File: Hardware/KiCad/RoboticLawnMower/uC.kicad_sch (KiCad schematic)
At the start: 9 parts, among them J12 Conn_02x05_Row_Letter_Last, U2 AVR128DB48x-xPT, Y1 32.768kHz

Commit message: Layout
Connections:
- net CURR_ALERT_CHRG: no longer names the net of U2.4 (PB0)
- net CURR_ALERT_M1: no longer names the net of U2.11 (PC1)
- net CURR_ALERT_M2: no longer names the net of U2.10 (PC0)
- net CURR_ALERT_M3: no longer names the net of U2.9 (PB5)
- net CURR_ALERT_M4: no longer names the net of U2.8 (PB4)
- net CURR_ALERT_M5: no longer names the net of U2.5 (PB1)
- net CURR_ALERT_SYS: no longer names the net of U2.3 (PA7)
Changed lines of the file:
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@@
   (junction (at 233.68 119.38) (diameter 0) (color 0 0 0 0)
-  )
-  (bus_entry (at 283.21 114.3) (size 2.54 2.54)
-    (stroke (width 0) (type default) (color 0 0 0 0))
-  )
-  (bus_entry (at 283.21 116.84) (size 2.54 2.54)
-    (stroke (width 0) (type default) (color 0 0 0 0))
-  )
-  (bus_entry (at 283.21 109.22) (size 2.54 2.54)
-    (stroke (width 0) (type default) (color 0 0 0 0))
-  )
-  (bus_entry (at 283.21 132.08) (size 2.54 2.54)
-    (stroke (width 0) (type default) (color 0 0 0 0))
-  )
-  (bus_entry (at 283.21 134.62) (size 2.54 2.54)
-    (stroke (width 0) (type default) (color 0 0 0 0))
-  )
-  (bus_entry (at 283.21 127) (size 2.54 2.54)
-    (stroke (width 0) (type default) (color 0 0 0 0))
-  )
-  (bus_entry (at 283.21 124.46) (size 2.54 2.54)
-    (stroke (width 0) (type default) (color 0 0 0 0))
   )
   (wire (pts (xy 100.33 60.96) (xy 110.49 60.96))
@@
   )
   (wire (pts (xy 233.68 71.12) (xy 233.68 72.39))
-    (stroke (width 0) (type default) (color 0 0 0 0))
-  )
-  (bus (pts (xy 285.75 129.54) (xy 285.75 134.62))
     (stroke (width 0) (type default) (color 0 0 0 0))
   )
@@
     (stroke (width 0) (type default) (color 0 0 0 0))
   )
-  (wire (pts (xy 220.98 114.3) (xy 283.21 114.3))
-    (stroke (width 0) (type default) (color 0 0 0 0))
-  )
-  (bus (pts (xy 285.75 116.84) (xy 285.75 119.38))
-    (stroke (width 0) (type default) (color 0 0 0 0))
-  )
   (wire (pts (xy 57.15 44.45) (xy 57.15 48.26))
     (stroke (width 0) (type default) (color 0 0 0 0))
@@
   )
   (wire (pts (xy 220.98 139.7) (xy 266.7 139.7))
-    (stroke (width 0) (type default) (color 0 0 0 0))
-  )
-  (wire (pts (xy 220.98 109.22) (xy 283.21 109.22))
     (stroke (width 0) (type default) (color 0 0 0 0))
   )
@@
     (stroke (width 0) (type default) (color 0 0 0 0))
   )
-  (bus (pts (xy 285.75 134.62) (xy 285.75 137.16))
-    (stroke (width 0) (type default) (color 0 0 0 0))
-  )
   (wire (pts (xy 198.12 163.83) (xy 200.66 163.83))
     (stroke (width 0) (type default) (color 0 0 0 0))
@@
     (stroke (width 0) (type default) (color 0 0 0 0))
   )
-  (wire (pts (xy 220.98 116.84) (xy 283.21 116.84))
-    (stroke (width 0) (type default) (color 0 0 0 0))
-  )
   (wire (pts (xy 87.63 99.06) (xy 180.34 99.06))
-    (stroke (width 0) (type default) (color 0 0 0 0))
-  )
-  (wire (pts (xy 220.98 132.08) (xy 283.21 132.08))
-    (stroke (width 0) (type default) (color 0 0 0 0))
-  )
-  (bus (pts (xy 285.75 119.38) (xy 285.75 127))
     (stroke (width 0) (type default) (color 0 0 0 0))
   )
@@
     (stroke (width 0) (type default) (color 0 0 0 0))
   )
-  (wire (pts (xy 220.98 134.62) (xy 283.21 134.62))
-    (stroke (width 0) (type default) (color 0 0 0 0))
-  )
   (wire (pts (xy 110.49 60.96) (xy 110.49 63.5))
-    (stroke (width 0) (type default) (color 0 0 0 0))
-  )
-  (wire (pts (xy 220.98 124.46) (xy 283.21 124.46))
     (stroke (width 0) (type default) (color 0 0 0 0))
   )
@@
     (stroke (width 0) (type default) (color 0 0 0 0))
   )
-  (bus (pts (xy 285.75 111.76) (xy 285.75 116.84))
-    (stroke (width 0) (type default) (color 0 0 0 0))
-  )
   (wire (pts (xy 220.98 119.38) (xy 233.68 119.38))
     (stroke (width 0) (type default) (color 0 0 0 0))
@@
     (stroke (width 0) (type default) (color 0 0 0 0))
   )
-  (bus (pts (xy 285.75 137.16) (xy 285.75 139.7))
-    (stroke (width 0) (type default) (color 0 0 0 0))
-  )
-  (wire (pts (xy 220.98 127) (xy 283.21 127))
-    (stroke (width 0) (type default) (color 0 0 0 0))
-  )
   (wire (pts (xy 82.55 55.88) (xy 88.9 55.88))
     (stroke (width 0) (type default) (color 0 0 0 0))
   )
   (wire (pts (xy 88.9 55.88) (xy 88.9 72.39))
-    (stroke (width 0) (type default) (color 0 0 0 0))
-  )
-  (bus (pts (xy 285.75 139.7) (xy 295.91 139.7))
     (stroke (width 0) (type default) (color 0 0 0 0))
   )
@@
     (stroke (width 0) (type default) (color 0 0 0 0))
   )
-  (bus (pts (xy 285.75 127) (xy 285.75 129.54))
-    (stroke (width 0) (type default) (color 0 0 0 0))
-  )
-  (label "CURR_ALERT_M3" (at 241.3 127 0)
-    (effects (font (size 1.27 1.27)) (justify left bottom))
-  )
-  (label "CURR_ALERT_M5" (at 241.3 116.84 0)
-    (effects (font (size 1.27 1.27)) (justify left bottom))
-  )
-  (label "CURR_ALERT_SYS" (at 241.3 109.22 0)
-    (effects (font (size 1.27 1.27)) (justify left bottom))
-  )
-  (label "CURR_ALERT_M2" (at 241.3 132.08 0)
-    (effects (font (size 1.27 1.27)) (justify left bottom))
-  )
   (label "AVR_UPDI" (at 45.72 58.42 0)
     (effects (font (size 1.27 1.27)) (justify left bottom))
   )
-  (label "CURR_ALERT_CHRG" (at 241.3 114.3 0)
-    (effects (font (size 1.27 1.27)) (justify left bottom))
-  )
-  (label "CURR_ALERT_M4" (at 241.3 124.46 0)
-    (effects (font (size 1.27 1.27)) (justify left bottom))
-  )
   (label "~{AVR_RERSET}" (at 123.19 60.96 0)
-    (effects (font (size 1.27 1.27)) (justify left bottom))
-  )
-  (label "CURR_ALERT_M1" (at 241.3 134.62 0)
     (effects (font (size 1.27 1.27)) (justify left bottom))
   )
@@
     (effects (font (size 1.27 1.27)) (justify left))
   )
-  (hierarchical_label "MOTOR_CONTROL" (shape bidirectional) (at 295.91 139.7 0)
-    (effects (font (size 1.27 1.27)) (justify left))
-  )

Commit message: LAYOUT
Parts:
- added C11: 5p6, Capacitor_SMD:C_0603_1608Metric, symbol Device:C
- added J18: Conn_02x05_Row_Letter_Last, Connector_PinHeader_1.27mm:PinHeader_2x05_P1.27mm_Vertical_SMD, symbol Connector_Generic:Conn_02x05_Odd_Even
- added R51, R53: 47K, Resistor_SMD:R_0603_1608Metric, symbol Device:R
- added R52: 33R, Resistor_SMD:R_0603_1608Metric, symbol Device:R
- added R54, R55: 4k7, Resistor_SMD:R_0603_1608Metric, symbol Device:R
- added R56, R57, R58, R60, R63: N.P., Resistor_SMD:R_0402_1005Metric, symbol Device:R
- added R59, R61, R62, R64, R65: 10R, Resistor_SMD:R_0402_1005Metric, symbol Device:R
- added U5: AVR128DB48x-xPT, Package_QFP:TQFP-48_7x7mm_P0.5mm, symbol MCU_Microchip_AVR_Dx:AVR128DB48x-xPT
- added Y2: 32.768kHz, Crystal:Crystal_SMD_3215-2Pin_3.2x1.5mm, symbol Device:Crystal
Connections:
- net +3.3V: now also J18.4 (Pin_4), R51.1, R53.1, R54.2, R55.2, U5.14 (VDDIO2), U5.28 (AVDD), U5.42 (VDD)
- net GND: now also C11.2, J18.2 (Pin_2), J18.9 (Pin_9), U5.15 (GND), U5.29 (AGND), U5.43 (GND)
- net I2C_1_SCL: now also R63.2, R64.2; no longer R42.1, U2.7 (PB3)
- net I2C_1_SDA: now also R59.2, R60.2; no longer R41.1, U2.6 (PB2)
- net Motor_M1..4_EN: now also R58.2, R65.2; no longer U2.13 (PC3)
- net Motor_M5_EN: now also R57.2, R62.2; no longer U2.16 (PC4)
- net ~{PCA_9685_OE}: now also R56.2, R61.2; no longer U2.12 (PC2)
- new net: R42.1, R63.1, U2.7 (PB3)
- new net: R56.1, U2.12 (PC2)
- new net: R41.1, R60.1, U2.6 (PB2)
- new net: R57.1, U2.16 (PC4)
- new net: R61.1, U5.12 (PC2)
- new net: R65.1, U5.13 (PC3)
- new net: R62.1, U5.16 (PC4)
- new net: U5.34 (XTAL32K1/PF0), Y2.2
- new net: U5.35 (XTAL32K2/PF1), Y2.1
- new net: R54.1, R59.1, U5.6 (PB2)
- new net: R55.1, R64.1, U5.7 (PB3)
- new net: J18.6 (Pin_6), R52.1
- new net: R58.1, U2.13 (PC3)
- new net AVR_UPDI_1: J18.3 (Pin_3), R51.2, U5.41 (UPDI)
- new net MOTOR_CTR_CTN_0: U5.21 (PD1)
- new net MOTOR_CTR_CTN_1: U5.22 (PD2)
- new net MOTOR_CTR_CTN_2: U5.23 (PD3)
- new net MOTOR_CTR_CTN_3: U5.24 (PD4)
- new net MOTOR_CTR_CTN_4: U5.20 (PD0)
- new net MOTOR_CTR_I2C_0_SCL: U5.47 (PA3)
- new net MOTOR_CTR_I2C_0_SDA: U5.46 (PA2)
- new net MOTOR_CTR_UART_0_RXD: U5.45 (XTALHF2/PA1)
- new net MOTOR_CTR_UART_0_TXD: U5.44 (XTALHF1/PA0)
- new net ~{AVR_RERSET_1}: C11.1, R52.2, R53.2, U5.40 (~{RESET}/PF6)
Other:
- moved on the sheet: R41, R42, U2, Y1

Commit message: bild hinzugefügt.
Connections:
- net MOTOR_CTR_UART_0_RXD is gone; now on an unnamed net: U5.45 (XTALHF2/PA1)
- net MOTOR_CTR_UART_0_TXD is gone; now on an unnamed net: U5.44 (XTALHF1/PA0)
- net UART_0_RXD: now also U2.1 (PA5); no longer U2.45 (XTALHF2/PA1)
- net UART_0_TXD: now also U2.48 (PA4); no longer U2.44 (XTALHF1/PA0)
- net ~{SMB_MUX_RESET}: now also U2.45 (XTALHF2/PA1); no longer U2.48 (PA4)
- net UART_0_XCK: now reaches U2.2 (PA6)
- net UART_0_XDIR: now reaches U2.3 (PA7)
- net MOTOR_CTR_I2C_0_SCL: no longer names the net of U5.47 (PA3)
- net MOTOR_CTR_I2C_0_SDA: no longer names the net of U5.46 (PA2)

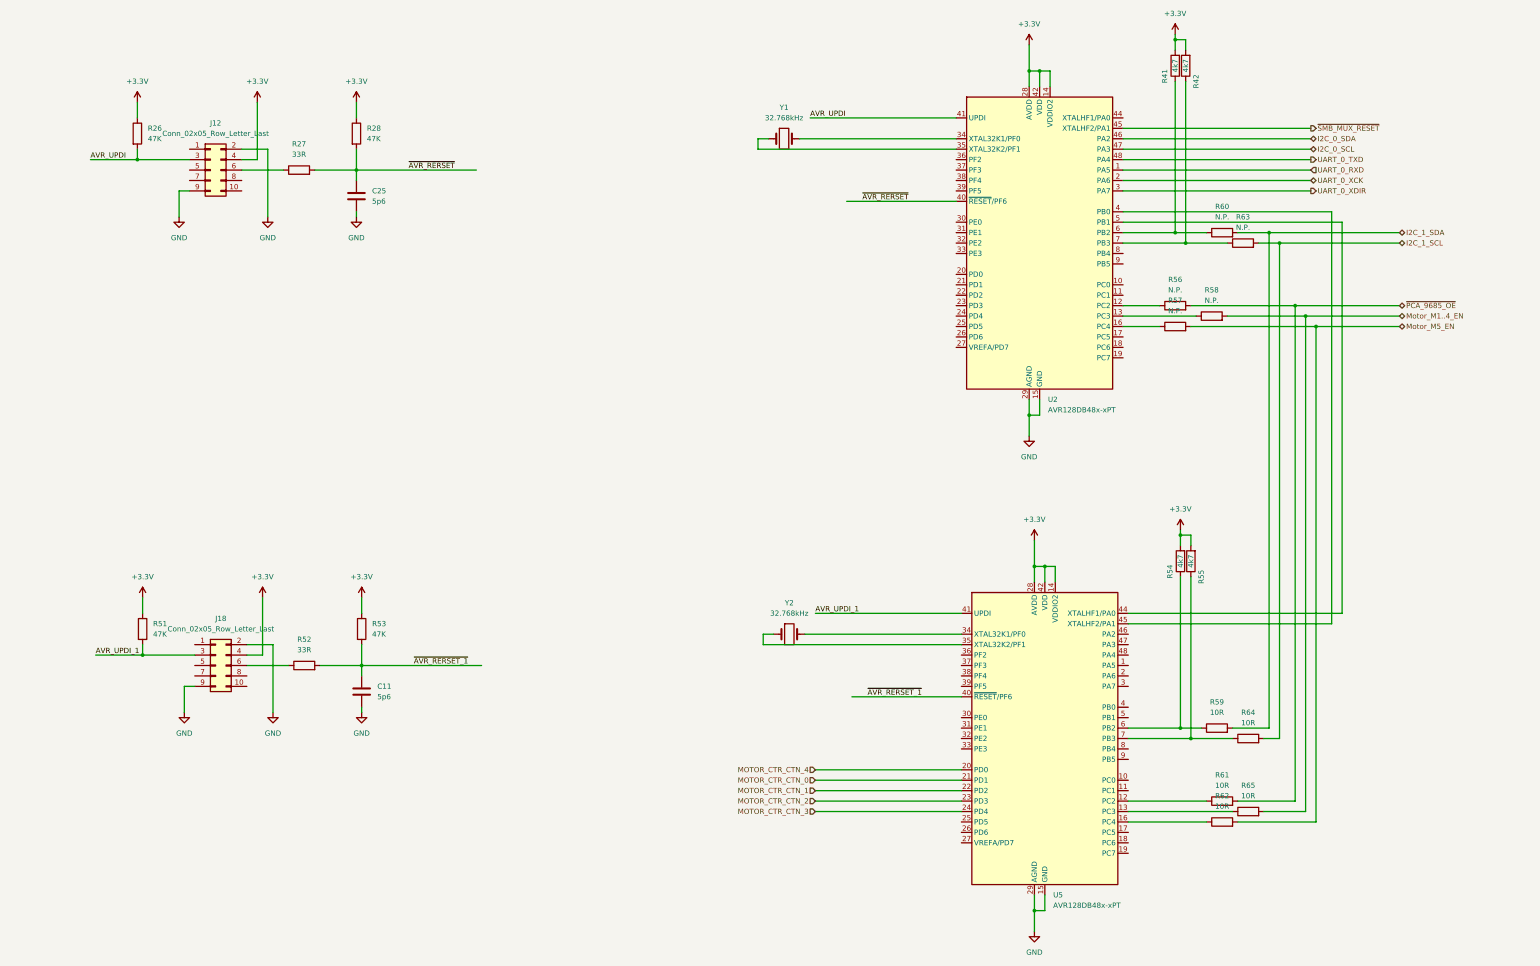
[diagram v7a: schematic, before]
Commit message: Schaltplan und Layout änderung
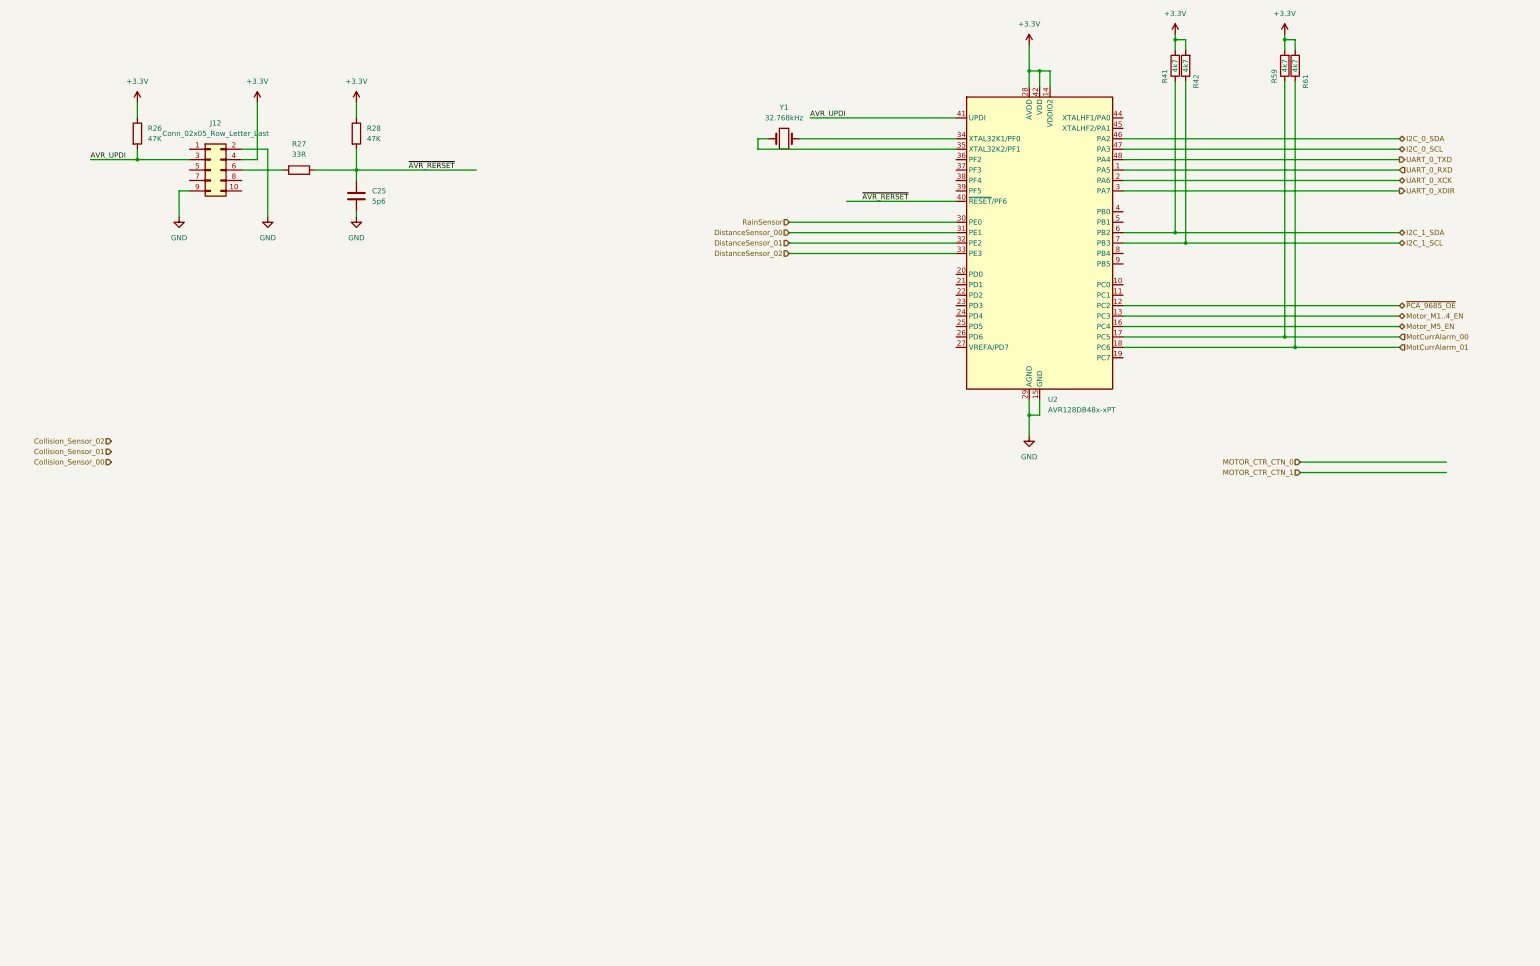
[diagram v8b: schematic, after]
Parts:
- removed C11: 5p6, Capacitor_SMD:C_0603_1608Metric, symbol Device:C
- removed J18: Conn_02x05_Row_Letter_Last, Connector_PinHeader_1.27mm:PinHeader_2x05_P1.27mm_Vertical_SMD, symbol Connector_Generic:Conn_02x05_Odd_Even
- removed R51, R53: 47K, Resistor_SMD:R_0603_1608Metric, symbol Device:R
- removed R52: 33R, Resistor_SMD:R_0603_1608Metric, symbol Device:R
- removed R54, R55: 4k7, Resistor_SMD:R_0603_1608Metric, symbol Device:R
- removed R56, R57, R58, R60, R63: N.P., Resistor_SMD:R_0402_1005Metric, symbol Device:R
- removed R62, R64, R65: 10R, Resistor_SMD:R_0402_1005Metric, symbol Device:R
- removed U5: AVR128DB48x-xPT, Package_QFP:TQFP-48_7x7mm_P0.5mm, symbol MCU_Microchip_AVR_Dx:AVR128DB48x-xPT
- removed Y2: 32.768kHz, Crystal:Crystal_SMD_3215-2Pin_3.2x1.5mm, symbol Device:Crystal
- R59, R61: value 10R -> 4k7; footprint Resistor_SMD:R_0402_1005Metric -> Resistor_SMD:R_0603_1608Metric
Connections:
- net +3.3V: now also R59.2, R61.2
- net I2C_1_SCL: now also R42.1, U2.7 (PB3)
- net I2C_1_SDA: now also R41.1, U2.6 (PB2); no longer R59.2
- net Motor_M1..4_EN: now also U2.13 (PC3)
- net Motor_M5_EN: now also U2.16 (PC4)
- net ~{PCA_9685_OE}: now also U2.12 (PC2); no longer R61.2
- net MotCurrAlarm_01: now reaches R61.1
- net MotCurrAlarm_01: now also U2.18 (PC6)
- net MotCurrAlarm_00: now reaches R59.1
- net MotCurrAlarm_00: now also U2.17 (PC5)
- net RainSensor: now reaches U2.30 (PE0)
- net DistanceSensor_00: now reaches U2.31 (PE1)
- net DistanceSensor_01: now reaches U2.32 (PE2)
- net DistanceSensor_02: now reaches U2.33 (PE3)
- net ~{SMB_MUX_RESET}: no longer names the net of U2.45 (XTALHF2/PA1)
